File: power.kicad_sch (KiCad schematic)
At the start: 55 parts, among them U2 TLP290-4(TPE, U23 LT3060ETS8-5#TRMPBF, U28 ACSL-6210-00RE, U30 NLVVHC1G126DFT1G

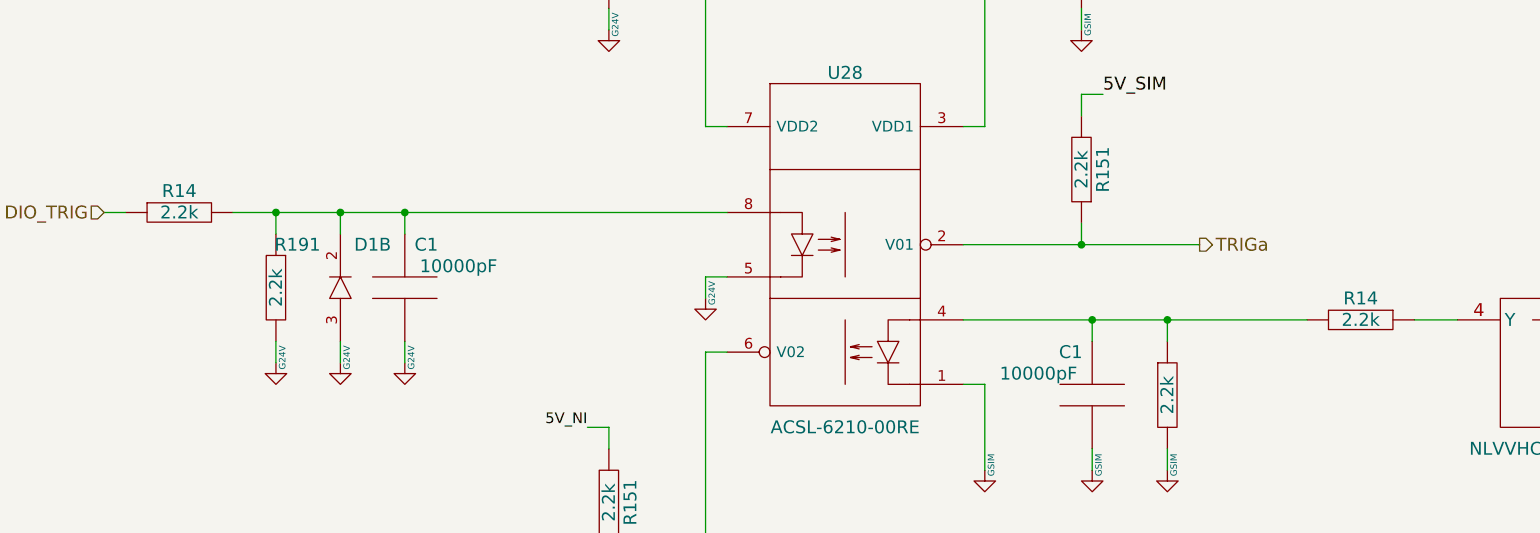
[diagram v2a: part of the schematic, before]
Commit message: - zero origin on so - silk - sch trig and rtsi lines need 510 resistor - assembly updated - sch and pcb project name and rev - no changes to gerber, old one can be used
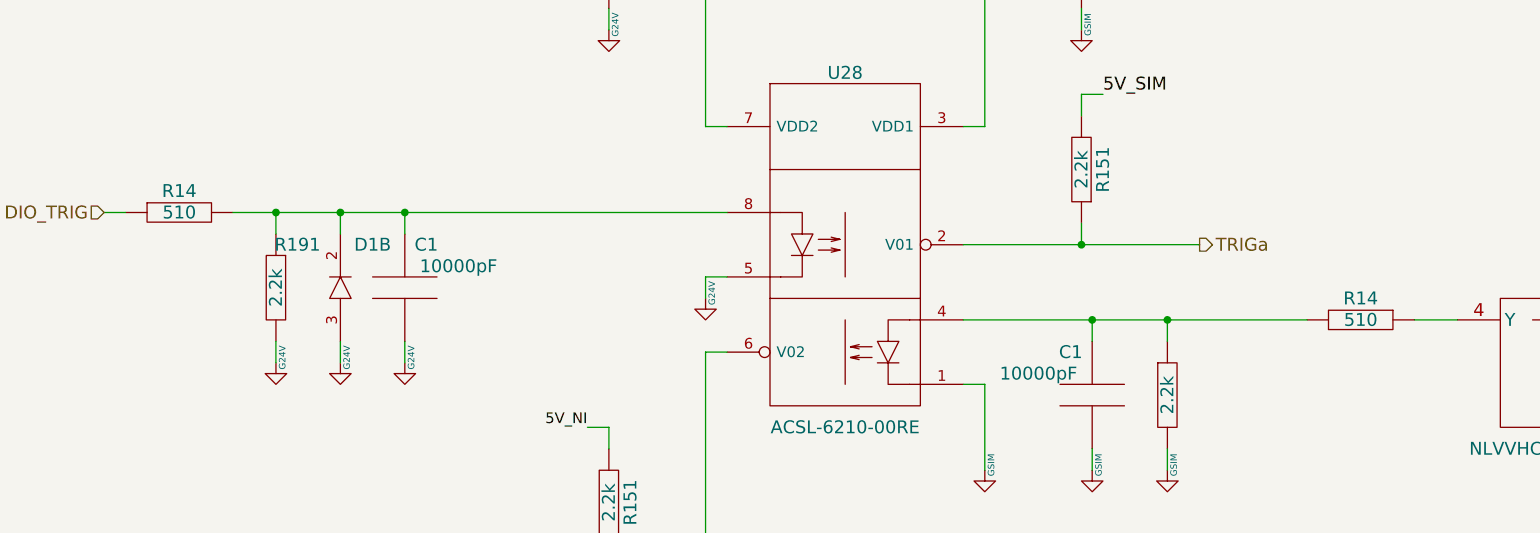
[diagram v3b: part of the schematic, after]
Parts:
- R14: value RC0603JR-072K2L -> RC0603FR-07510RL; symbol Resistor_Yageo:RC0603JR-072K2L -> Resistor_Yageo:RC0603FR-07510RL; ManufacturerPartNumber RC0603JR-072K2L -> RC0603FR-07510RL; Nominal 2.2k -> 510; SupplierPartNumber 311-2.2KGRCT-ND -> 311-510HRCT-ND; Tolerance 5% -> (none)
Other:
- title: EOL ECU POWER CARD -> EOL ECU MIX CARD
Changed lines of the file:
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@@
   (paper "A3")
   (title_block
-    (title "EOL ECU POWER CARD")
-    (date "2023-04-03")
-    (rev "0B")
+    (title "EOL ECU MIX CARD")
+    (date "2023-09-26")
+    (rev "0C")
     (company "ARXTRON TECHNOLOGIES")
     (comment 1 "A0180-V0")

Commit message: dnp res for di pwr dnp led feed for 5v replace with 6.49k feed for ign_on on sim circuit
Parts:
- R? (x2): value RC0603FR-07220RL -> RC0603FR-076K49L; symbol Resistor_Yageo:RC0603FR-07220RL -> Resistor_Yageo:RC0603FR-076K49L; ManufacturerPartNumber RC0603FR-07220RL -> RC0603FR-076K49L; Nominal 220 -> 6.49K; SupplierPartNumber 311-220HRTR-ND -> 311-6.49KHRCT-ND
